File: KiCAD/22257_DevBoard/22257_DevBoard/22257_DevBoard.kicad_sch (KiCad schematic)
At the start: 0 parts

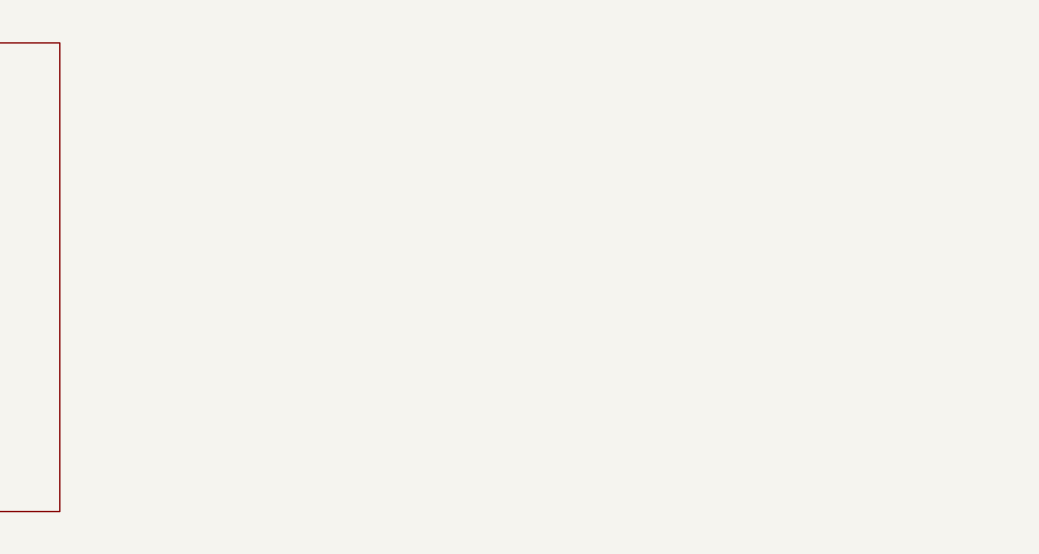
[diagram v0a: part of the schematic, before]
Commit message: Schematic Progress. Added connections to the MicroZed and added a 3v3 rail regulator
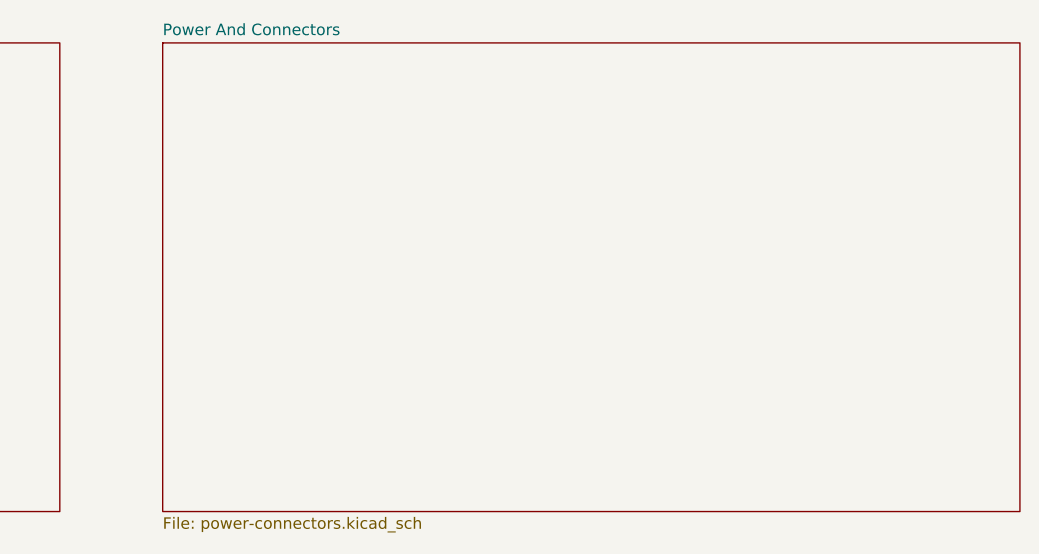
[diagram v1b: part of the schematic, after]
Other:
- added sheet Power And Connectors (power-connectors.kicad_sch)
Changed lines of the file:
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@@
+	)
+	(sheet
+		(at 219.71 19.05)
+		(size 95.25 52.07)
+		(exclude_from_sim no)
+		(in_bom yes)
+		(on_board yes)
+		(dnp no)
+		(fields_autoplaced yes)
+		(stroke
+			(width 0.1524)
+			(type solid)
+		)
+		(fill
+			(color 0 0 0 0.0000)
+		)
+		(property "Sheetname" "Power And Connectors"
+			(at 219.71 18.3384 0)
+			(effects
+				(font
+					(size 1.27 1.27)
+				)
+				(justify left bottom)
+			)
+		)
+		(property "Sheetfile" "power-connectors.kicad_sch"
+			(at 219.71 71.7046 0)
+			(effects
+				(font
+					(size 1.27 1.27)
+				)
+				(justify left top)
+			)
+		)
+		(instances
+			(project "22257_DevBoard"
+				(path "/271303ce-366a-4ce1-87f0-a9575f73ea97"
+					(page "4")
+				)
+			)
+		)
 	)
 	(sheet

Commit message: Done :D
Existence is pain
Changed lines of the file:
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@@
 	(paper "A3")
 	(image
-		(at 146.05 189.23)
+		(at 208.28 179.07)
 		(scale 0.724029)
 		(data "iVBORw0KGgoAAAANSUhEUgAABKcAAAK6CAYAAADsGD8CAAAAAXNSR0IArs4c6QAAAARnQU1BAACx"
@@
 			"AAAAAAAAAAAAAAAAAAAAAAAAAAAAAAAAAAAAAAAAAAAAAAAAAAAAAAAAAAAAAAAAAAAAAAAAAAAA"
 			"AAAAAAAAAAAAAAAAAAAAAAAAAAAAAAAAAAAAAAAAAAAAAAAAAAAAAAAAAAAAAAAAAAAAAAAAAAAA"
+			"AAAAAAAAAAAAAAAAAAAAAAAAAAAAAAAAAAAAAAAAAAAAAAAAAAAAAAAAAAAAAAAAAAAAAAAAAAAA"
+			"AAAAAAAAAAAAAAAAAAAAAAAAAAAAAAAAAAAAAAAAAAAAAAAAAAAAAAAAAAAAAAAAAAAAAAAAAAAA"
+			"AAAAAAAAAAAAAAAAAAAAAAAAAAAAAAAAAAAAAAAAAAAAAAAAAAAAAAAAAAAAAAAAAAAAAAAAAAAA"
+			"AAAAAAAAAAAAAAAAAAAAAAAAAAAAAAAAAAAAAAAAAAAAAAAAAAAAAAAAAAAAAAAAAAAAAAAAAAAA"
+			"AAAAAAAAAAAAAAAAAAAAAAAAAAAAAAAAAAAAAAAAAAAAAAAAAAAAAAAAAAAAAAAAAAAAAAAAAAAA"
+			"AAAAAAAAAAAAAAAAAAAAAAAAAAAAAAAAAAAAAAAAAAAAAAAAAAAAAAAAAAAAAAAAAAAAAAAAAAAA"
+			"AAAAAAAAAAAAAAAAAAAAAAAAAAAAAAAAAAAAAAAAAAAAAAAAAAAAAAAAAAAAAAAAAAAAAAAAAAAA"
+			"AAAAAAAAAAAAAAAAAAAAAAAAAAAAAAAAAAAAAAAAAAAAAAAAAAAAAAAAAAAAAAAAAAAAAAAAAAAA"
+			"AAAAAAAAAAAAAAAAAAAAAAAAAAAAAAAAAAAAAAAAAAAAAAAAAAAAAAAAAAAAAAAAAAAAAAAAAAAA"
+			"AAAAAAAAAAAAAAAAAAAAAAAAAAAAAAAAAAAAAAAAAAAAAAAAAAAAAAAAAAAAAAAAAAAAAAAAAAAA"
+			"AAAAAAAAAAAAAAAAAAAAAAAAAAAAAAAAAAAAAAAAAAAAAAAAAAAAAAAAAAAAAAAAAAAAAAAAAAAA"
+			"AAAAAAAAAAAAAAAAAAAAAAAAAAAAAAAAAAAAAAAAAAAAAAAAAAAAAAAAAAAAAAAAAAAAAAAAAAAA"
+			"AAAAAAAAAAAAAAAAAAAAAAAAAAAAAAAAAAAAAAAAAAAAAAAAAAAAAAAAAAAAAAAAAAAAAAAAAAAA"
+			"AAAAAAAAAAAAAAAAAAAAAAAAAAAAAAAAAAAAAAAAAAAAAAAAAAAAAAAAAAAAAAAAAAAAAAAAAAAA"
+			"AAAAAAAAAAAAAAAAAAAAAAAAAAAAAAAAAAAAAAAAAAAAAAAAAAAAAAAAAAAAAAAAAAAAAAAAAAAA"
+			"AAAAAAAAAAAAAAAAAAAAAAAAAAAAAAAAAAAAAAAAAAAAAAAAAAAAAAAAAAAAAAAAAAAAAAAAAAAA"
+			"AAAAAAAAAAAAAAAAAAAAAAAAAAAAAAAAAAAAAAAAAAAAAAAAAAAAAAAAAAAAAAAAAAAAAAAAAAAA"
+			"AAAAAAAAAAAAAAAAAAAAAAAAAAAAAAAAAAAAAAAAAAAAAAAAAAAAAAAAAAAAAAAAAAAAAAAAAAAA"
 			"AAAAAAAAAAAAAAAAAAAAAAAAAA=="
 		)
 	)
 	(sheet
-		(at 219.71 19.05)
+		(at 266.7 45.72)
 		(size 95.25 52.07)
 		(exclude_from_sim no)
@@
 		)
 		(property "Sheetname" "Power And Connectors"
-			(at 219.71 18.3384 0)
+			(at 266.7 45.0084 0)
 			(effects
 				(font
-					(size 1.27 1.27)
+					(size 2.54 2.54)
 				)
 				(justify left bottom)
@@
 		)
 		(property "Sheetfile" "power-connectors.kicad_sch"
-			(at 219.71 71.7046 0)
+			(at 266.7 98.3746 0)
 			(effects
 				(font
@@
 	)
 	(sheet
-		(at 24.13 19.05)
+		(at 49.53 45.72)
 		(size 77.47 52.07)
 		(exclude_from_sim no)
@@
 		)
 		(property "Sheetname" "MicroZed_Headers"
-			(at 24.13 18.3384 0)
+			(at 49.53 45.0084 0)
 			(effects
 				(font
-					(size 1.27 1.27)
+					(size 2.54 2.54)
 				)
 				(justify left bottom)
@@
 		)
 		(property "Sheetfile" "Microzed_Headers.kicad_sch"
-			(at 24.13 71.7046 0)
+			(at 49.53 98.3746 0)
 			(effects
 				(font
@@
 	)
 	(sheet
-		(at 128.27 19.05)
+		(at 158.75 45.72)
 		(size 80.01 52.07)
 		(exclude_from_sim no)
@@
 		)
 		(property "Sheetname" "Oscillators"
-			(at 128.27 18.3384 0)
-			(show_name yes)
+			(at 158.75 44.3734 0)
 			(effects
 				(font
-					(size 1.27 1.27)
+					(size 2.54 2.54)
 				)
 				(justify left bottom)
@@
 		)
 		(property "Sheetfile" "oscillators.kicad_sch"
-			(at 128.27 71.7046 0)
+			(at 158.75 98.3746 0)
 			(effects
 				(font
